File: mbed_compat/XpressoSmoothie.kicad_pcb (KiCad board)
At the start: 2 copper layers, 99.7 x 99.7 mm, 119 parts, among them J1 HEADER_4, J10 HEADER_3X2, J11 Pwr_in, J12 HEADER_4, J13 HEADER_4X2, J14 HEADER_3X2, J15 HEADER_4, J16 HEADER_3, J17 HEADER_3, J18 HEADER_3, J19 HEADER_2, J2 HEADER_4, J20 HEADER_2, J21 HEADER_2, J22 HEADER_2, J23 HEADER_3, J24 HEADER_3, J25 HEADER_3, J26 USB, J27 HEADER_4, J28 MICROSD-MOLEX, J3 HEADER_3, J4 HEADER_3X2, J5 HEADER_3X2, J6 LPCXPRESSO_GENERIC_HEADER, J7 HEADER_4, J8 HEADER_4, J9 HEADER_3X2, M1 LOGO_OSHW, M2 LOGO_OSHW, Q1 IRLB 8743, Q2 IRLB 8743, Q3 IRLB 8743, Q4 IRLB 8743, SW1 SW_PUSH, SW2 SW_PUSH, U1 POLOLU_A4988, U10 TC4422A, U11 TC4422A, U12 LM1117-3.3, U2 POLOLU_A4988, U3 POLOLU_A4988, U4 POLOLU_A4988, U5 POLOLU_A4988, U7 LM7812CT, U8 TC4422A, U9 TC4422A

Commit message: latest changes
latest changes
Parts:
- added JP4: JUMPER-2, PIN_ARRAY_2X1, F.Cu at (156.2, 89.5)
- added JP5: JUMPER-2, PIN_ARRAY_2X1, F.Cu at (162.2, 89.5)
- moved JP3 10.2 mm to (161.3, 121.3)
- moved C1 2.25 mm to (75.2, 114.6), turned to 90 degrees
- moved C9 2.22 mm to (118.7, 103.2)
- moved J27 1.93 mm to (153.0, 125.1)
- moved C10 1.91 mm to (125.1, 103.5)
- moved C11 1.91 mm to (131.4, 103.5)
- moved J15 1.00 mm to (141.3, 125.1)
- moved M2 0.71 mm to (143.2, 101.6)
- moved J13 0.32 mm to (129.5, 126.4)
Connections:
- net Vin renamed Vin_rmot
- Hole1 pad 1: N-00000131 -> (no net)
- Hole2 pad 1: N-00000128 -> (no net)
- Hole3 pad 1: N-00000130 -> (no net)
- Hole4 pad 1: N-00000129 -> (no net)
- J16 pad 3: VCC -> +5V
- J17 pad 3: VCC -> +5V
- J18 pad 3: VCC -> +5V
- J23 pad 3: VCC -> +5V
- J24 pad 3: VCC -> +5V
- J25 pad 3: VCC -> +5V
- J28 pad 1: N-0000045 -> (no net)
- J28 pad 8: N-0000043 (its old number) -> (no net)
- J6 pad 2: +5V -> VIN
- J6 pad 29: N-00000124 (its old number) -> +5V
- J6 pad 3: N-00000127 -> VBAT
- J6 pad 30: N-00000126 -> (no net)
- J6 pad 31: N-00000125 (its old number) -> (no net)
- JP3 pad 1: VCC -> 3V3IN
- JP3 pad 2: 3V3IN -> VCC
- U10 pad 3: N-0000058 -> (no net)
- U11 pad 3: N-0000056 -> (no net)
- U8 pad 3: N-0000038 -> (no net)
- U9 pad 3: N-0000039 -> (no net)
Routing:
- net +5V: track 76.6 -> 154.8 mm, vias 3 -> 4
- net Vgates: track 150.9 -> 228.1 mm, vias 3 -> 4
- net VCC: track 398.7 -> 327.0 mm
- net GND: track 798.8 -> 783.6 mm
- net Vin_rmot: track 330.5 -> 317.1 mm
- net RESET: track 16.2 -> 22.2 mm
- net VBAT: track 0.00 -> 5.76 mm
- net VIN: track 0.00 -> 4.58 mm
- net CS: track 40.5 -> 38.2 mm
- net THERM2: track 34.2 -> 32.0 mm
- net THERM1: track 44.7 -> 42.8 mm
- net THERM0: track 57.4 -> 55.5 mm
- net XMAX: track 21.5 -> 23.1 mm
- net YMAX: track 25.6 -> 27.1 mm
- net SDA: track 14.0 -> 12.6 mm
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
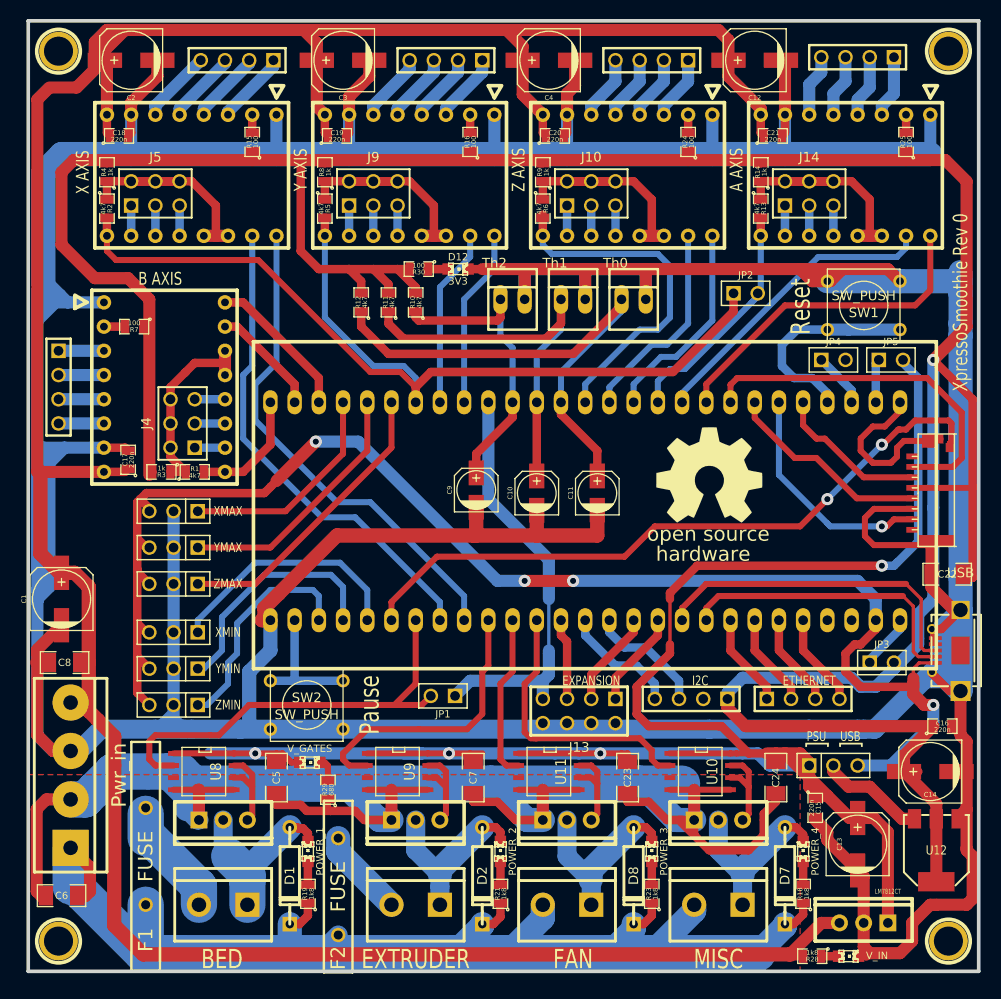
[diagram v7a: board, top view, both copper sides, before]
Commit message: endstops jumper
endstops jumper
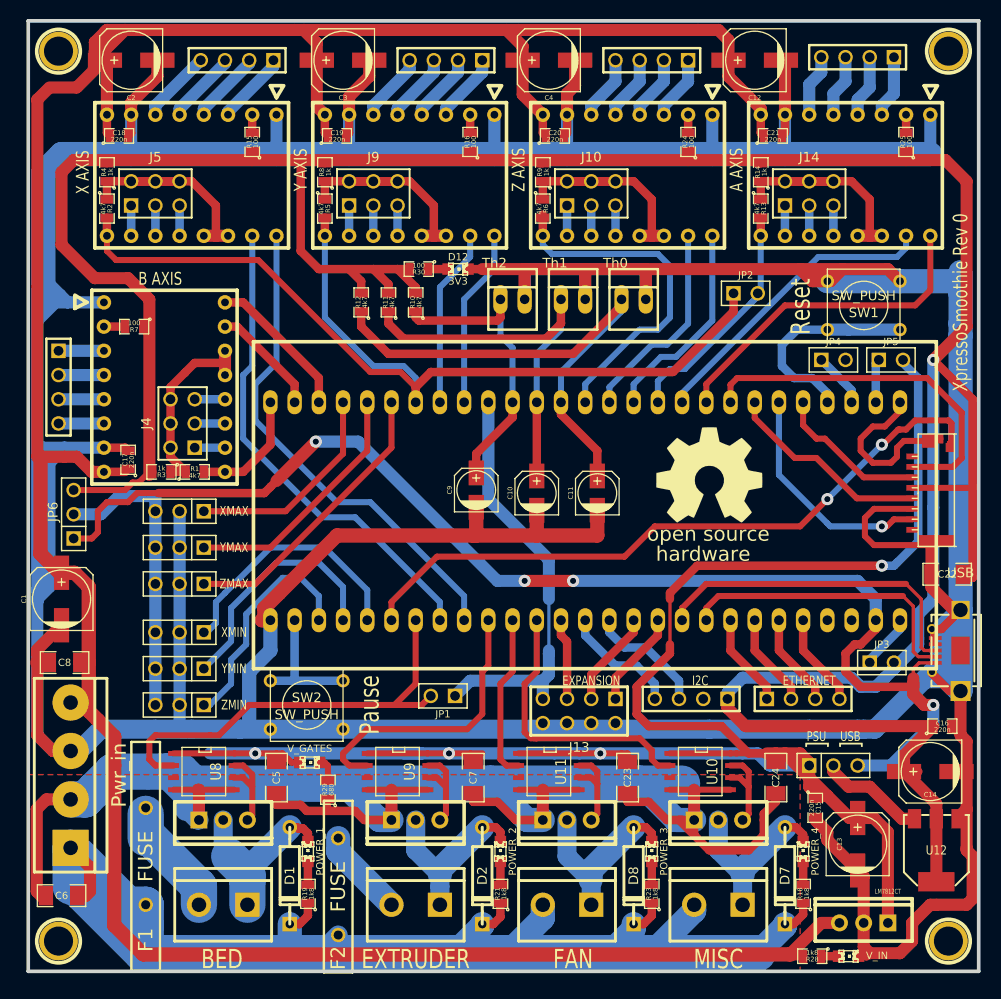
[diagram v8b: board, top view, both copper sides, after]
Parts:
- added JP6: JUMPER-3, PIN_ARRAY_3X1, F.Cu at (76.5, 105.7)
- moved J16 0.63 mm to (87.6, 118.1)
- moved J17 0.63 mm to (87.6, 105.4)
- moved J18 0.63 mm to (87.6, 121.9)
- moved J23 0.63 mm to (87.6, 109.2)
- moved J24 0.63 mm to (87.6, 125.7)
- moved J25 0.63 mm to (87.6, 113.0)
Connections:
- net VCC renamed +3.3VP
- J16 pad 3: +5V -> /E+
- J17 pad 3: +5V -> /E+
- J18 pad 3: +5V -> /E+
- J23 pad 3: +5V -> /E+
- J24 pad 3: +5V -> /E+
- J25 pad 3: +5V -> /E+
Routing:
- net /E+: track 0.00 -> 31.3 mm
- net GND: track 783.6 -> 759.7 mm
- net +5V: track 154.8 -> 133.0 mm
- net Vin_Hi_curr: track 141.9 -> 163.6 mm
- net +3.3VP: track 327.0 -> 336.8 mm
- net XMIN: track 25.9 -> 27.1 mm
- net Vin_rmot: track 317.1 -> 317.8 mm
- net ZMAX: track 31.0 -> 30.4 mm
- net YMAX: track 27.1 -> 26.4 mm
- net XMAX: track 23.1 -> 22.5 mm
